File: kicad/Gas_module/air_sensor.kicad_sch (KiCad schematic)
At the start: 24 parts, among them J1 Program Header, M1 MiCS-6814, U9 Buffer

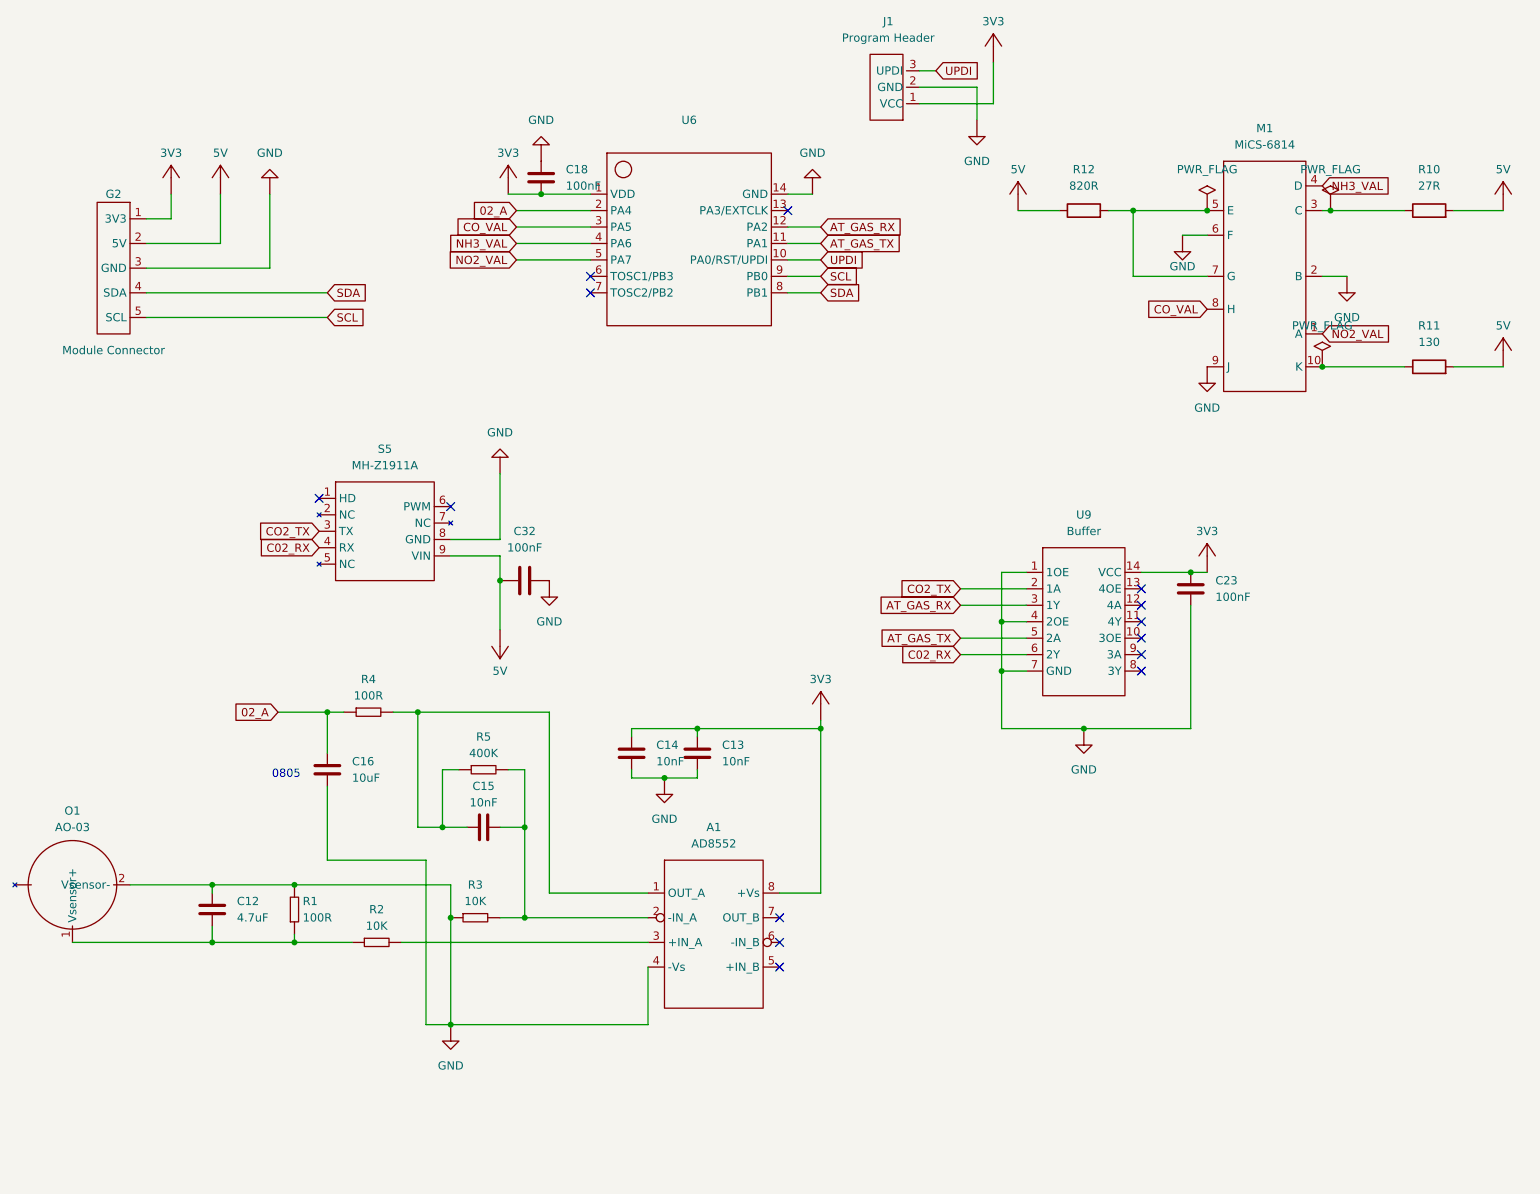
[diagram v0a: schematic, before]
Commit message: added pcb for gas and climate modules
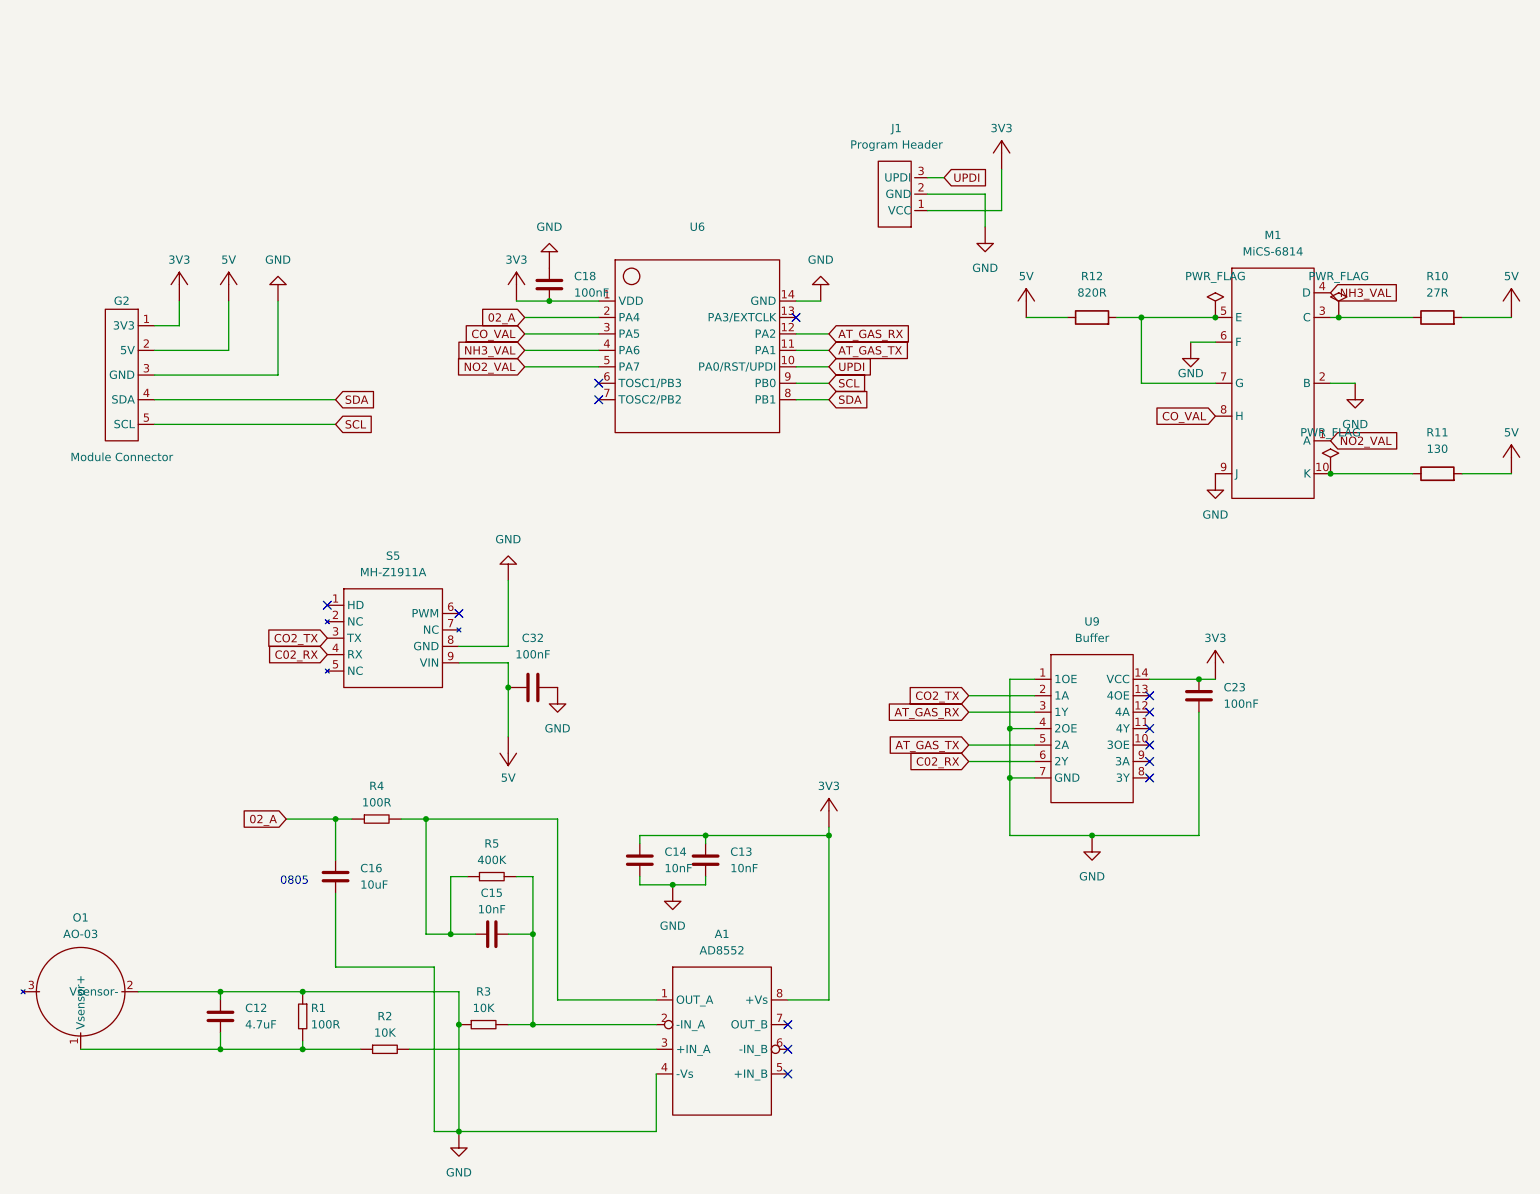
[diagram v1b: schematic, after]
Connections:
- net GND: now also R1.1; no longer R1.2
- net at C12.1, O1.1 (Vsensor+), R2.1: now also R1.2; no longer R1.1
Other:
- moved on the sheet: A1, C12, C13, C14, C15, C16, C18, C23, C32, G2, J1, M1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

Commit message: added status LED to gas module
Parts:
- added D1: ~, common:LED_3mm_THT, symbol common:LED
- added R6: 220, common:R_0603, symbol common:Resistor
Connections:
- net GND: now also D1.1 (K)
- net STATUS_LED: now reaches U6.7 (TOSC2/PB2)
- net STATUS_LED: now also R6.1
- new net: D1.2 (A), R6.2
- no-connect marks 14 -> 13

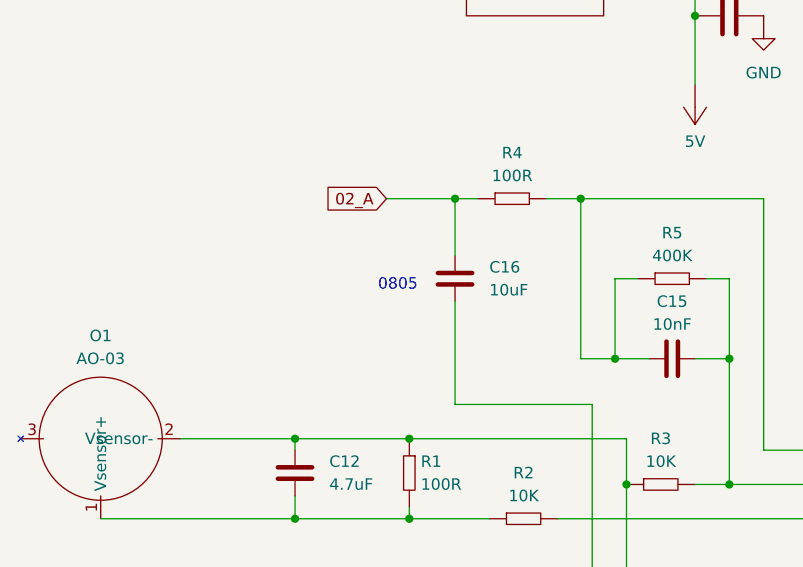
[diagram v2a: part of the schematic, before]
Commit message: added 1206 smd capacitor footprint
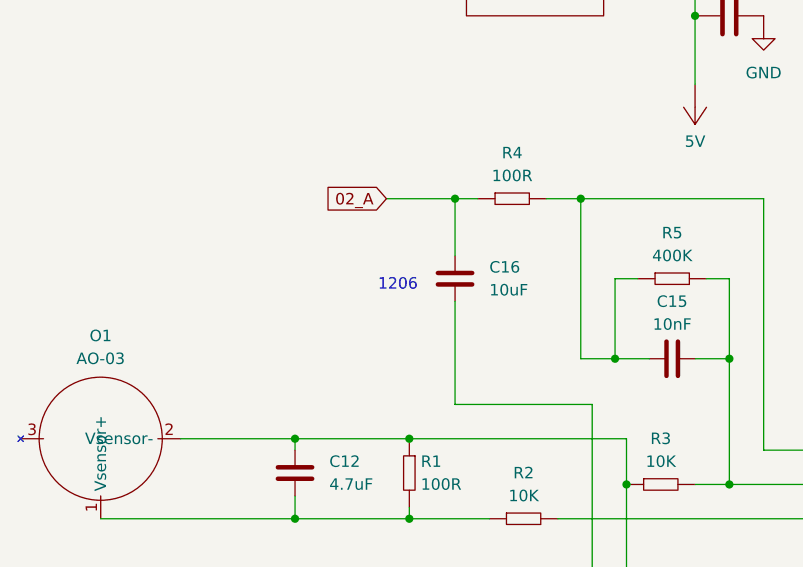
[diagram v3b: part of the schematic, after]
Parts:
- C16: footprint common:C_0805 -> common:C_1206
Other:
- note added: "1206"
- note removed: "0805"
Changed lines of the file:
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@@
 	(generator_version "9.0")
 	(paper "A4")
-	(text "0805"
+	(text "1206"
 		(exclude_from_sim no)
 		(at 71.12 148.082 0)
@@
 			)
 		)
-		(property "Footprint" "common:C_0805"
+		(property "Footprint" "common:C_1206"
 			(at 77.47 147.32 0)
 			(effects
